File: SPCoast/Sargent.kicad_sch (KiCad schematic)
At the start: 43 parts, among them SW13001 835, SW13003 1, SW13835 835

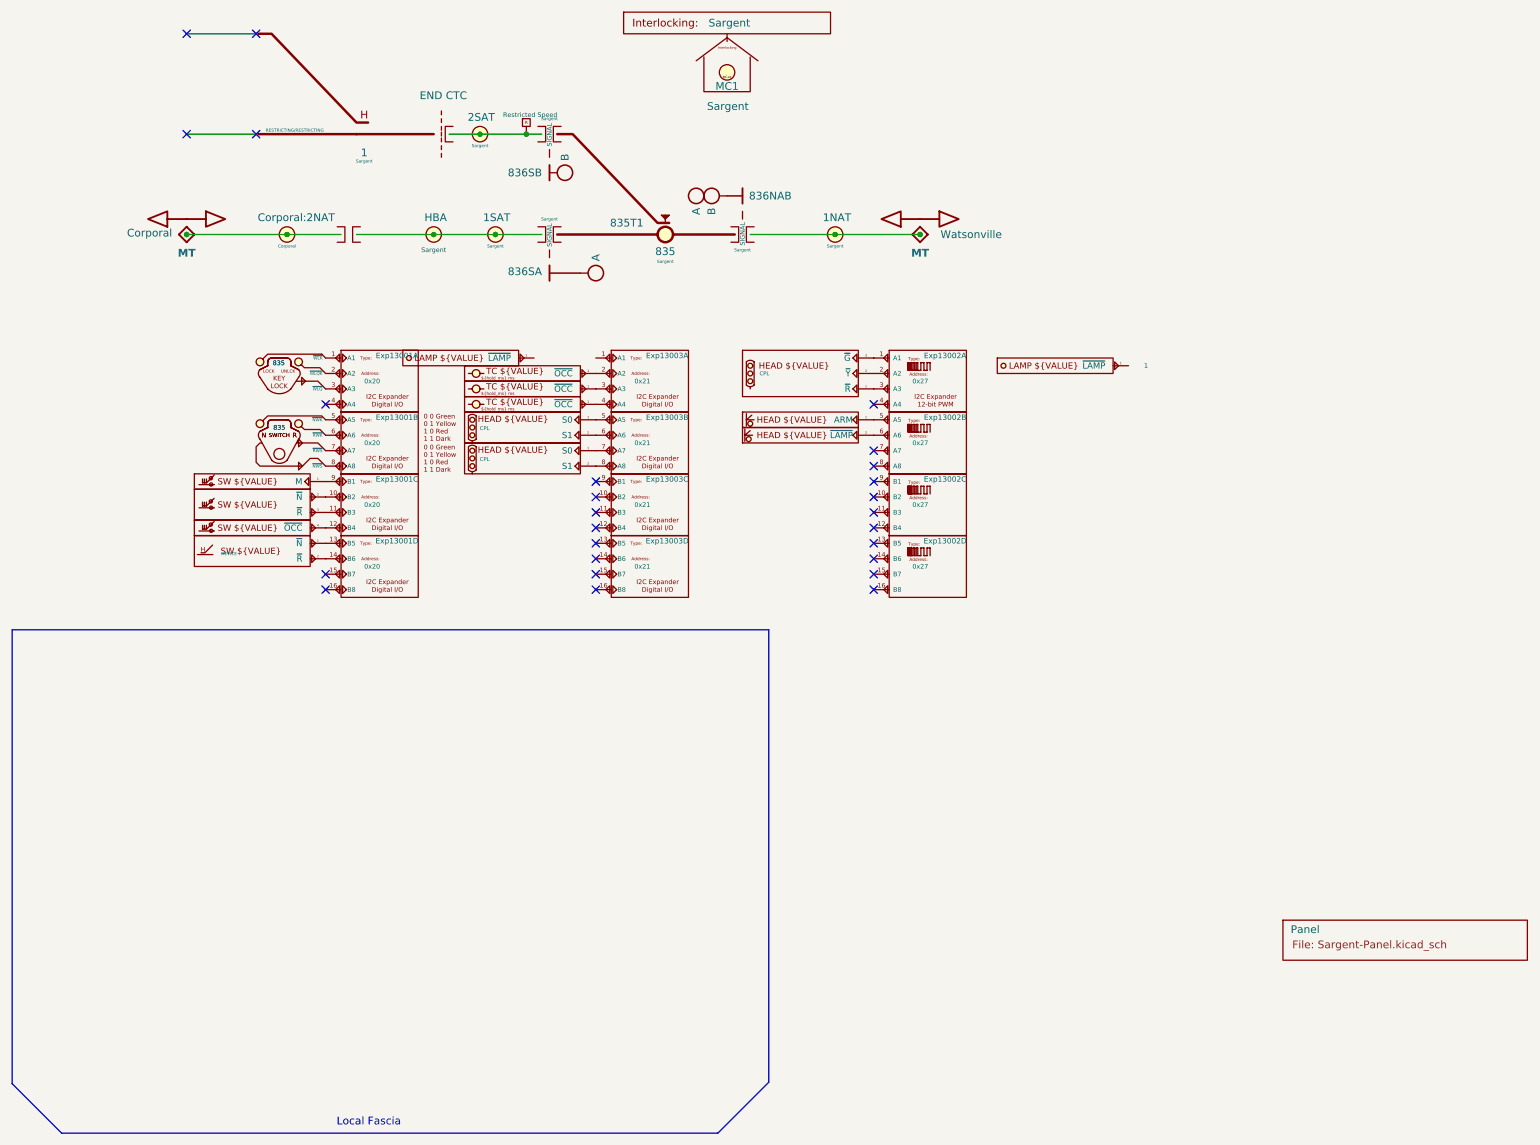
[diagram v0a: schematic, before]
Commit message: chore: owner's Sargent cleanup and library edits of 2026-10-12 and 13 (baseline)
Co-Authored-By: Claude Fable 5.1 <noreply@anthropic.com>
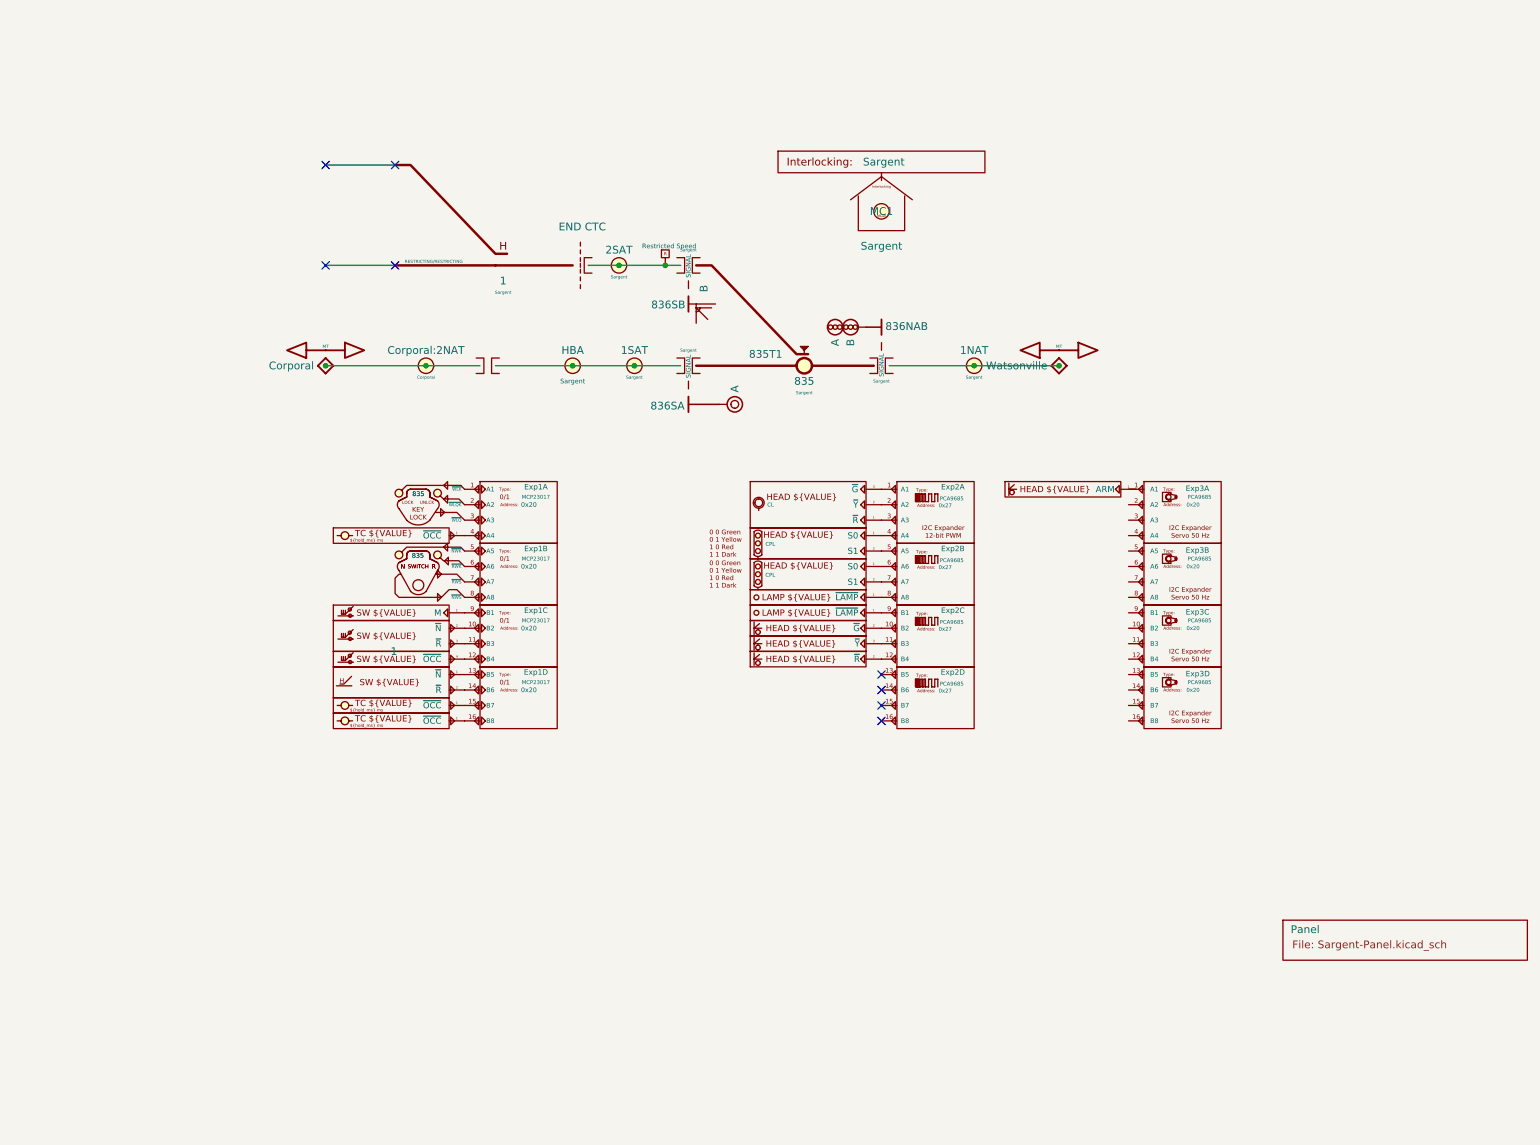
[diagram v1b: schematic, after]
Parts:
- removed DevSW1: 836NA, symbol Railroad-Field:Device-Head-CPL-Encoder
- removed DevSW13008: 1NAT, symbol Railroad-Field:Device-TrackCircuit-Optical
- removed DevSW13009: 1SAT, symbol Railroad-Field:Device-TrackCircuit-Optical
- removed DevSW13010: 2SAT, symbol Railroad-Field:Device-TrackCircuit-Optical
- removed DevSW13012: MC1, symbol Railroad-Field:Device-Lamp
- removed DevSW13013: HBA, symbol Railroad-Field:Device-Lamp
- removed DevSW3: 836NB, symbol Railroad-Field:Device-Head-CPL-Encoder
- removed DevSW4: 836SA, symbol Railroad-Field:Device-Head-CPL
- removed DevSW5: (no value), symbol Railroad-Field:Device-Head-Semaphore-UQ
- removed Exp13003: ${ADDRESS}, symbol Railroad-HardwareIO:Driver-I2C-MCP23017
- added DevSW1: 1NAT, symbol Railroad-Field:Device-TrackCircuit-Optical
- added DevSW10: MC1, symbol Railroad-Field:Device-Lamp
- added DevSW11: HBA, symbol Railroad-Field:Device-Lamp
- added DevSW3: 1SAT, symbol Railroad-Field:Device-TrackCircuit-Optical
- added DevSW4: 2SAT, symbol Railroad-Field:Device-TrackCircuit-Optical
- added DevSW6: 836SA, symbol Railroad-Field:Device-Head-CL_3
- added DevSW7: 836NA, symbol Railroad-Field:Device-Head-CPL-Encoder
- added DevSW8: 836NB, symbol Railroad-Field:Device-Head-CPL-Encoder
- added DevSW9: 836SB, symbol Railroad-Field:Device-Head-Semaphore-UQ-CL_3
- added Exp3: ${ADDRESS}, symbol Railroad-HardwareIO:Driver-I2C-PCA9685-Servo
- H1: renamed from H13004; symbol Railroad-Trackplan:Signal Head - CPL -> Railroad-Trackplan:Signal Head - SemaphoreUQ3
- H2: renamed from H13003; symbol Railroad-Trackplan:Signal Head - CPL -> Railroad-Trackplan:Signal Head - CL
- renumbered AUX13001 to AUX1, B13001 to B1, B13002 to B2, B13003 to B3, B13004 to B4, B13005 to B5, CP13002 to CP1, CP13001 to CP2, DOT13004 to DOT1, DOT13006 to DOT2, DOT13005 to DOT3, DevSW13002 to DevSW2, DevSW2 to DevSW5, Exp13001 to Exp1, Exp13002 to Exp2, H13001 to H3, H13002 to H4, HOUSE13001 to HOUSE1, LK13001 to LK2, MC13001 to MC1, Plant13001 to Plant1, S13003 to S1, S13002 to S2, S13001 to S3, SW13001 to SW2, SW13003 to SW3, SW13835 to SW4, TC13004 to TC1, TC13002 to TC2, TC13001 to TC3, TC13005 to TC4
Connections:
- net at Exp2.5 (A5): now also DevSW7.2 (S1)
- net at Exp2.6 (A6): now also DevSW8.1 (S0)
- net at Exp2.7 (A7): now also DevSW8.2 (S1)
- net at Exp2.8 (A8): now also DevSW10.1 (~{LAMP})
- net at Exp1.4 (A4): now also DevSW1.1 (~{OCC})
- net at Exp1.15 (B7): now also DevSW3.1 (~{OCC})
- net at Exp1.16 (B8): now also DevSW4.1 (~{OCC})
- net at Exp2.1 (A1): now also DevSW6.3 (~{G})
- net at Exp2.2 (A2): now also DevSW6.2 (~{Y})
- net at Exp2.3 (A3): now also DevSW6.1 (~{R})
- net at Exp2.4 (A4): now also DevSW7.1 (S0)
- net at Exp2.10 (B2): now also DevSW9.2 (~{G})
- net at Exp2.11 (B3): now also DevSW9.3 (~{Y})
- net at Exp2.12 (B4): now also DevSW9.2 (~{R})
- net at Exp2.9 (B1): now also DevSW11.1 (~{LAMP})
- no-connect marks 26 -> 8
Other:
- note removed: "Local Fascia"
- moved on the sheet: Exp2A, Exp2B, Exp2C, Exp2D

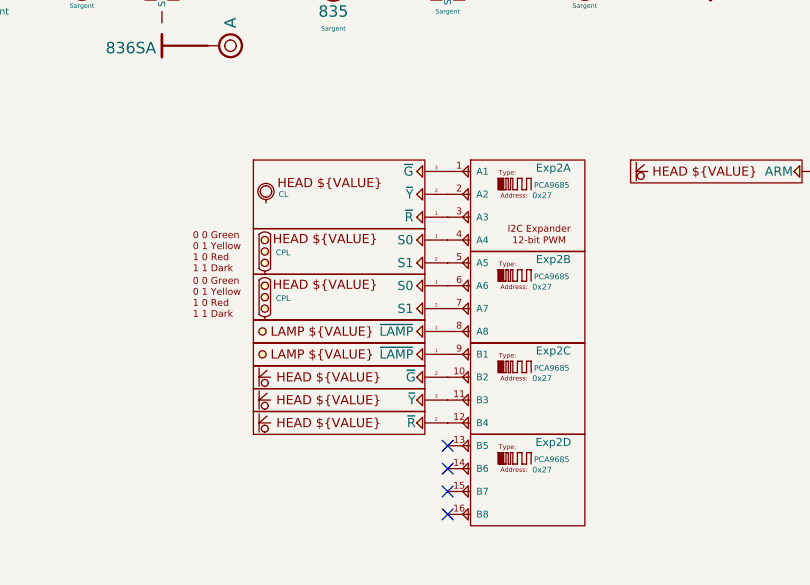
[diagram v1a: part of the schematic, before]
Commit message: feat(symbols): the six-head set; field layout closed; Local plates are devices; reference prefixes by kind
Owner's rulings 2026-10-13 (Subdivision checkpoint E71 to E73). Railroad-Field by
symbols/edits/2026-10-13-head-set.py: Device-Head-CL (legs R, G, B; yellow is R plus G),
Device-Head-CL-Pixel (one RGB color point), Device-Head-Semaphore (Style "LQ, UQ"; LAMP is a
color point: pixel direct, white lamp by cast), Device-Head-Semaphore-RGB (ARM plus R, G, B),
beside Device-Head-CPL and -CPL-Encoder; the LQ, UQ binary-lamp devices and Local-Lamp gone;
Local-Switch and Local-Lock Role DEVICE; the owner's Adapter-Color-3Lamp withdrawn with the
adapter design. Reference prefixes DevHead, DevLamp, DevSW, DevLock, DevTC, DevContact.
Sargent remapped by the migration script (symbol renames, Pin.* synced) and its devices
re-referenced by kind (836SA is DevHead1, 836SB is DevHead4).

Verified: lint 82 symbols, 0 errors; netlist gate against the baseline, references ignored:
connectivity identical; ERC only Sargent's 17 unwired servo channels and the semaphore arm.

Co-Authored-By: Claude Fable 5.1 <noreply@anthropic.com>
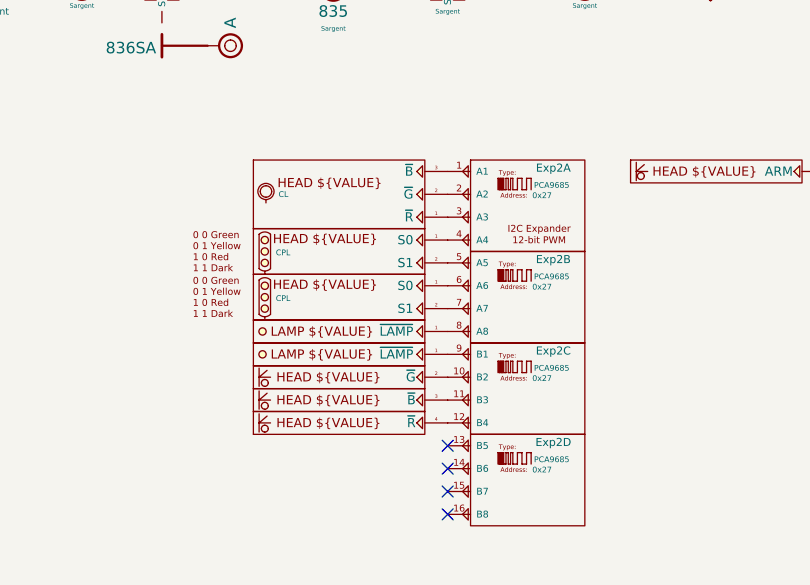
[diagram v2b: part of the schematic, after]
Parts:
- DevHead1: renamed from DevSW6; symbol Railroad-Field:Device-Head-CL_3 -> Railroad-Field:Device-Head-CL; Pin.B (none) -> binary; Pin.Y binary -> (none)
- DevHead4: renamed from DevSW9; symbol Railroad-Field:Device-Head-Semaphore-UQ-CL_3 -> Railroad-Field:Device-Head-Semaphore-RGB; Pin.B (none) -> binary; Pin.G (none) -> binary; Pin.LAMP color -> (none); Pin.R (none) -> binary
- H1: symbol Railroad-Trackplan:Signal Head - SemaphoreUQ3 -> Railroad-Trackplan:Signal Head - Semaphore-UQ
- renumbered DevSW7 to DevHead2, DevSW8 to DevHead3, DevSW10 to DevLamp1, DevSW11 to DevLamp2, DevSW1 to DevTC1, DevSW3 to DevTC2, DevSW4 to DevTC3
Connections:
- net at Exp2.12 (B4): now also DevHead4.4 (~{R}); no longer DevHead4.2 (~{R})

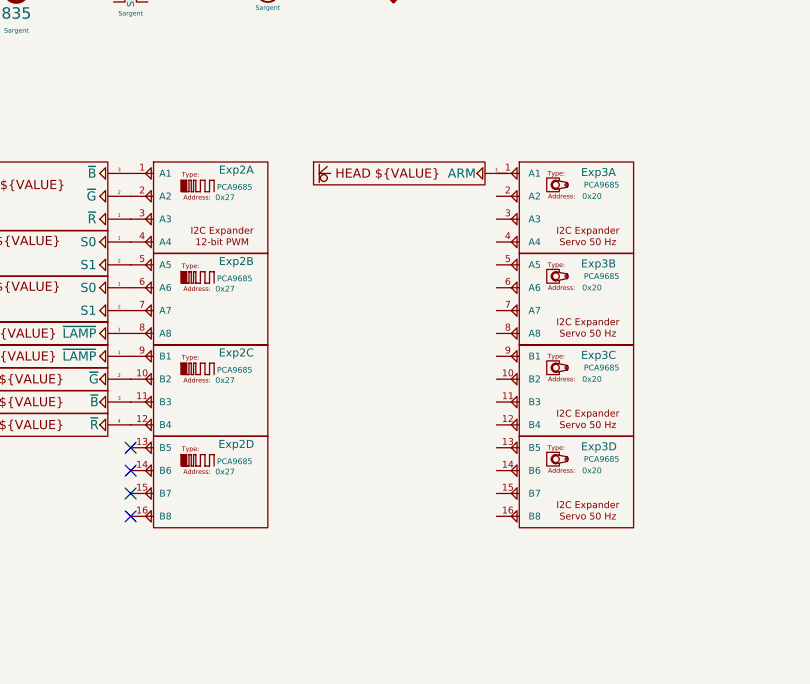
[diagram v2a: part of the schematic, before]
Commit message: feat(spcoast): Sargent's semaphore arm wired to the servo chip; ERC clean
Owner's edit in KiCad, 2026-10-16. Verified: ERC clean across the project; netlist gate against
the previous commit shows one net gained (the arm to the PCA9685-Servo channel) and nothing else.

Co-Authored-By: Claude Fable 5.1 <noreply@anthropic.com>
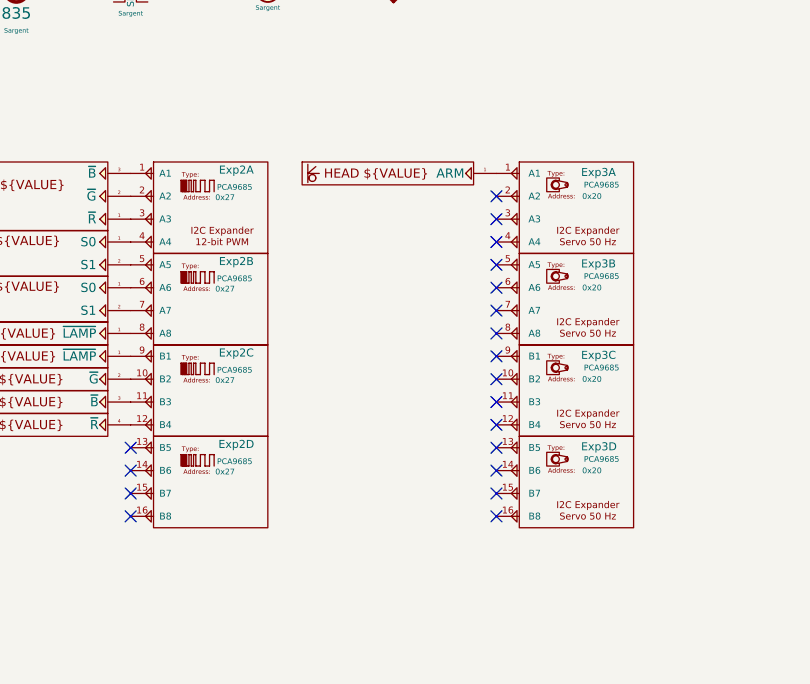
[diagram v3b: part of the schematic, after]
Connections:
- net at Exp3.1 (A1): now also DevHead4.1 (ARM)
- no-connect marks 8 -> 23
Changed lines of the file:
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@@
 	)
 	(no_connect
+		(at 200.66 124.46)
+	)
+	(no_connect
+		(at 200.66 114.3)
+	)
+	(no_connect
+		(at 200.66 99.06)
+	)
+	(no_connect
 		(at 68.58 40.64)
 	)
 	(no_connect
+		(at 200.66 101.6)
+	)
+	(no_connect
 		(at 160.02 129.54)
 	)
@@
 	)
 	(no_connect
+		(at 200.66 127)
+	)
+	(no_connect
+		(at 200.66 96.52)
+	)
+	(no_connect
+		(at 200.66 121.92)
+	)
+	(no_connect
+		(at 200.66 106.68)
+	)
+	(no_connect
 		(at 160.02 132.08)
 	)
@@
 	)
 	(no_connect
+		(at 200.66 119.38)
+	)
+	(no_connect
+		(at 200.66 109.22)
+	)
+	(no_connect
 		(at 80.01 40.64)
 	)
 	(no_connect
+		(at 200.66 132.08)
+	)
+	(no_connect
+		(at 200.66 129.54)
+	)
+	(no_connect
+		(at 200.66 104.14)
+	)
+	(no_connect
 		(at 160.02 127)
 	)
+	(no_connect
+		(at 200.66 116.84)
+	)
+	(no_connect
+		(at 200.66 111.76)
+	)
 	(wire
 		(pts
@@
 	(symbol
 		(lib_id "Railroad-Field:Device-Head-Semaphore-RGB")
-		(at 201.93 95.25 0)
+		(at 200.66 95.25 0)
 		(unit 1)
 		(body_style 1)
@@
 		(fields_autoplaced yes)
 		(property "Reference" "DevHead4"
-			(at 195.6216 92.0952 0)
+			(at 194.3516 92.0952 0)
 			(hide yes)
 			(show_name no)
@@
 		)
 		(property "Value" "836SB"
-			(at 201.93 95.25 0)
+			(at 200.66 95.25 0)
 			(hide yes)
 			(show_name no)
@@
 		)
 		(property "Footprint" ""
-			(at 201.93 95.25 0)
+			(at 200.66 95.25 0)
 			(hide yes)
 			(show_name no)
@@
 		)
 		(property "Datasheet" ""
-			(at 201.93 95.25 0)
+			(at 200.66 95.25 0)
 			(hide yes)
 			(show_name no)
@@
 		)
 		(property "Description" "Semaphore head with an RGB LED behind the roundel-less lens: ARM position; legs R, G, B as the color light head (E71)."
-			(at 203.073 116.078 0)
+			(at 201.803 116.078 0)
 			(hide yes)
 			(show_name no)
@@
 		)
 		(property "Role" "DEVICE"
-			(at 192.151 90.932 0)
+			(at 190.881 90.932 0)
 			(hide yes)
 			(show_name no)
@@
 		)
 		(property "stop_deg" ""
-			(at 201.93 95.25 0)
+			(at 200.66 95.25 0)
 			(hide yes)
 			(show_name no)
@@
 		)
 		(property "approach_deg" ""
-			(at 201.93 95.25 0)
+			(at 200.66 95.25 0)
 			(hide yes)
 			(show_name no)
@@
 		)
 		(property "clear_deg" ""
-			(at 201.93 95.25 0)
+			(at 200.66 95.25 0)
 			(hide yes)
 			(show_name no)
@@
 		)
 		(property "Appliance" "head"
-			(at 191.77 92.075 0)
+			(at 190.5 92.075 0)
 			(hide yes)
 			(show_name no)
@@
 		)
 		(property "Style" "UQ"
-			(at 194.818 90.932 0)
+			(at 193.548 90.932 0)
 			(hide yes)
 			(show_name no)
@@
 		)
 		(property "Pin.ARM" "position"
-			(at 206.756 91.313 0)
+			(at 205.486 91.313 0)
 			(hide yes)
 			(show_name no)
@@
 		)
 		(property "Pin.B" "binary"
-			(at 201.93 95.25 0)
+			(at 200.66 95.25 0)
 			(hide yes)
 			(show_name no)
@@
 		)
 		(property "Pin.G" "binary"
-			(at 201.93 95.25 0)
+			(at 200.66 95.25 0)
 			(hide yes)
 			(show_name no)
@@
 		)
 		(property "Pin.R" "binary"
-			(at 201.93 95.25 0)
+			(at 200.66 95.25 0)
 			(hide yes)
 			(show_name no)
@@
 		)
 		(property "ki_locked" ""
-			(at 201.93 95.25 0)
+			(at 200.66 95.25 0)
 			(hide yes)
 			(show_name no)
@@
 		(pin "2"
 		)
-		(pin "2"
+		(pin "4"
 		)
 		(instances
@@
 		(pin "2"
 		)
-		(pin "2"
+		(pin "4"
 		)
 		(instances
@@
 		(pin "2"
 		)
-		(pin "2"
+		(pin "4"
 		)
 		(instances
@@
 		(pin "1"
 		)
-		(pin "2"
+		(pin "4"
 		)
 		(pin "2"

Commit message: fix(spcoast): placed instances agree with their library symbols on Role, Appliance, Style
KiCad copies fields at placement and never follows the library. The 2026-10-12 migration
filled empty instance fields but kept non-empty ones, so heads placed before the libraries
were corrected still said Role COMPONENT and Style CPL. A compiler joining devices to
appliances by Appliance and Style (I9) would have failed on Sargent's CL and UQ heads.

The one-off `SPCoast/edits/2026-10-16-sync-library-fields.py` sets every library-owned
field (Role, Appliance, Style, IC, Kind, Pin.*) on every instance of a Railroad-* symbol
to the library's value, by text edit. 58 instances on 7 sheets: 53 heads to Role APPLIANCE
(Sargent's H1 to Style UQ and H2 to CL), two Mileposts to Role TRACK (ADR 0004 D7), the
Sargent Local plates to Role DEVICE (checkpoint E72), and 836SB's semaphore device to the
library's Style list `LQ, UQ`.

Front-end rule this records (owner, 2026-10-16): library-owned fields are read from the
library by lib_id, and an instance that disagrees is a diagnostic.

Verified:
- tools/contract/netlist_diff.py production/SPCoast.net production/post-sync.net: 493 nets,
  1086 nodes, 485 parts, connectivity identical
- kicad-cli sch erc --severity-all: 0 violations
- the script re-run reports 0 changes

Co-Authored-By: Claude Fable 5.1 <noreply@anthropic.com>
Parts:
- DevHead4: Style UQ -> LQ, UQ
- H1: Role COMPONENT -> APPLIANCE; Style CPL -> UQ
- H2: Role COMPONENT -> APPLIANCE; Style CPL -> CL
- H3, H4: Role COMPONENT -> APPLIANCE
- LK2, SW2: Role PANEL -> DEVICE
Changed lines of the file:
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@@
 			)
 		)
-		(property "Role" "PANEL"
+		(property "Role" "DEVICE"
 			(at 84.455 119.38 0)
 			(hide yes)
@@
 			)
 		)
-		(property "Role" "PANEL"
+		(property "Role" "DEVICE"
 			(at 83.185 90.17 0)
 			(hide yes)
@@
 			)
 		)
-		(property "Role" "COMPONENT"
+		(property "Role" "APPLIANCE"
 			(at 132.08 77.47 0)
 			(hide yes)
@@
 			)
 		)
-		(property "Style" "CPL"
+		(property "Style" "CL"
 			(at 132.08 77.47 0)
 			(hide yes)
@@
 			)
 		)
-		(property "Role" "COMPONENT"
+		(property "Role" "APPLIANCE"
 			(at 127 60.96 0)
 			(hide yes)
@@
 			)
 		)
-		(property "Style" "CPL"
+		(property "Style" "UQ"
 			(at 127 60.96 0)
 			(hide yes)
@@
 			)
 		)
-		(property "Role" "COMPONENT"
+		(property "Role" "APPLIANCE"
 			(at 156.21 69.85 0)
 			(hide yes)
@@
 			)
 		)
-		(property "Role" "PANEL"
+		(property "Role" "DEVICE"
 			(at 84.455 119.38 0)
 			(hide yes)
@@
 			)
 		)
-		(property "Role" "COMPONENT"
+		(property "Role" "APPLIANCE"
 			(at 158.75 69.85 0)
 			(hide yes)
@@
 			)
 		)
-		(property "Style" "UQ"
+		(property "Style" "LQ, UQ"
 			(at 193.548 90.932 0)
 			(hide yes)
@@
 			)
 		)
-		(property "Style" "UQ"
+		(property "Style" "LQ, UQ"
 			(at 152.908 111.252 0)
 			(hide yes)
@@
 			)
 		)
-		(property "Role" "PANEL"
+		(property "Role" "DEVICE"
 			(at 83.185 90.17 0)
 			(hide yes)
@@
 			)
 		)
-		(property "Style" "UQ"
+		(property "Style" "LQ, UQ"
 			(at 152.908 111.252 0)
 			(hide yes)
@@
 			)
 		)
-		(property "Style" "UQ"
+		(property "Style" "LQ, UQ"
 			(at 152.908 111.252 0)
 			(hide yes)
